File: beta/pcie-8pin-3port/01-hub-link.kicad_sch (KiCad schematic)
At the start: 6 parts, among them J1 TO-HUB

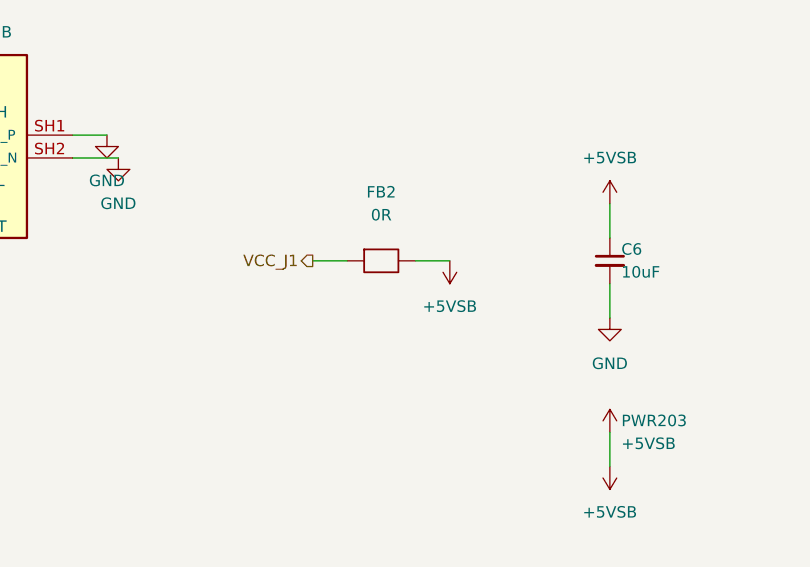
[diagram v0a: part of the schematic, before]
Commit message: pcie-8pin-3port: USB-ingress TPS2121 mux replaces the D2 SS34 ORing diode (spec v1.6.0 Sec 6.14)
Identical delta and topology to pcie-8pin-2port (docs/usb-ingress-bom-delta-2026-07-24.md
Sec 3.2; see that board's commit for the full rationale) -- the two boards' 07-usb-flash and
01-hub-link leaf sheets share the same coordinates, hierarchical_label mechanics for FB1's
"VBUS_J5" stub, and refdes plan (verified independently against the live pcie-3port file
before running, not assumed from the 2-port board). U4 = TPS2121RUXR: IN1 = RJ-45 VCC feed
after FB2 via a cross-sheet global_label "VCC_RJ45"; IN2 = VBUS behind new polyfuse F1 ahead
of the existing FB1 bead; OUT = +5VSB. OV1/PR1 dividers off IN1; CP2/OV2/GND -> GND; ST left
a genuine no_connect (Output-type pin, avoids the same pin_to_pin ERROR class recorded on
the other two boards). D2 removed entirely; refdes shifted R13->R14.../C41->C42... on the
same pre-existing-part collision as EPS/2-port.

Gates: ERC 122->133, zero new errors (pin_not_driven=1 unchanged pre-existing), pin_to_pin
stays 63, lib_symbol_mismatch +11 (same benign class). Netlist-verified clean on the first
run: +5VSB gains U4.1/U4.8 with no D2 member; /VBUS={C43,C44,C9,D3,D4,FB1.2,U4.2};
/VBUS_J5={F1.1,J5x4}; VCC_RJ45(global)={FB2.2,R15.1,R17.1,U4.7}. BOM regenerated via
scripts/gen-bom-outputs.py --force.

Co-Authored-By: Claude Fable 5 <noreply@anthropic.com>
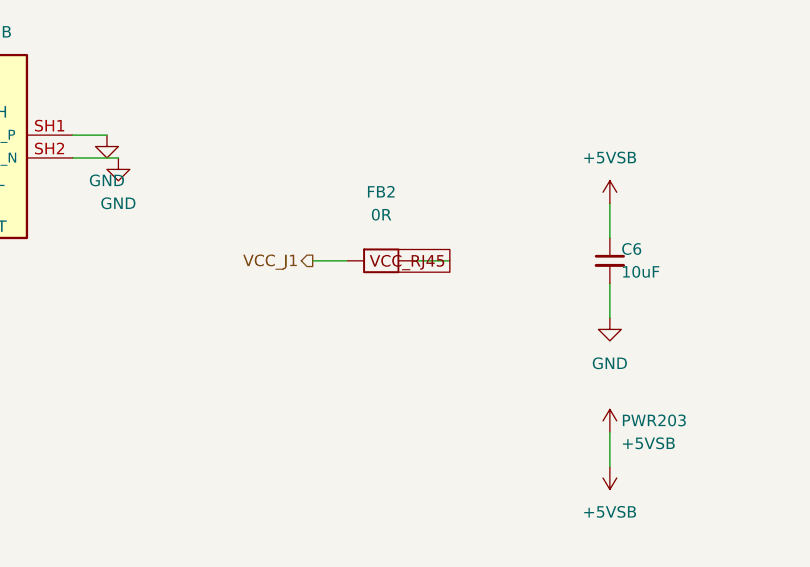
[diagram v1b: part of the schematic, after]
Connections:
- net +5VSB: no longer FB2.2
- new net VCC_RJ45: FB2.2
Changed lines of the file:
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@@
-	(symbol
-		(lib_id "cec-power:+5VSB")
-		(at 185.42 102.87 180)
-		(unit 1)
-		(exclude_from_sim no)
-		(in_bom yes)
-		(on_board yes)
-		(dnp no)
-		(property "Reference" "#PWR108" (at 185.42 100.33 0) (effects (font (size 1.27 1.27)) (hide yes)))
-		(property "Value" "+5VSB" (at 185.42 107.95 0) (effects (font (size 1.27 1.27))))
-		(pin "1")
-		(instances
-			(project "pcie8pin-3port-module"
-				(path "/a8ecf94e-f41a-4523-8cf1-1d72f47f3e7e/67f50ca3-8cb0-4aa6-9a3f-011faa4ff8d7" (reference "#PWR108") (unit 1))
-			)
-		)
-	)
 	(symbol
 		(lib_id "cec-power:+5VSB")
@@
 	(no_connect (at 123.19 91.44))
 	(no_connect (at 123.19 96.52))
+	(global_label "VCC_RJ45"
+		(shape passive)
+		(at 185.42 102.87 180)
+		(fields_autoplaced yes)
+		(effects (font (size 1.27 1.27)) (justify right bottom))
+		(property "Intersheetrefs" "${INTERSHEET_REFS}"
+			(at 185.42 102.87 0)
+			(effects (font (size 1.27 1.27)) (hide yes))
+		)
+	)
 	(sheet_instances
 		(path "/67f50ca3-8cb0-4aa6-9a3f-011faa4ff8d7"
